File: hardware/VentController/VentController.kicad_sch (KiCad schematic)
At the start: 21 parts

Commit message: Better labels
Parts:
- C1: value (none) -> 1uF; footprint (none) -> Capacitor_SMD:C_0805_2012Metric_Pad1.18x1.45mm_HandSolder
- C2: value (none) -> .1uF; footprint (none) -> Capacitor_SMD:C_0805_2012Metric_Pad1.18x1.45mm_HandSolder
- C3: footprint (none) -> Capacitor_SMD:C_0805_2012Metric_Pad1.18x1.45mm_HandSolder
- H1: value (none) -> MountingHole_Pad; footprint (none) -> MountingHole:MountingHole_2.5mm_Pad
- H2: footprint (none) -> MountingHole:MountingHole_2.5mm_Pad
- J1: value (none) -> AM2301B; footprint (none) -> Connector_PinHeader_2.54mm:PinHeader_1x04_P2.54mm_Vertical
- J2: value (none) -> Conn_01x02; footprint (none) -> Connector_PinHeader_2.54mm:PinHeader_1x02_P2.54mm_Vertical
- J3: value (none) -> Barrel_Jack_Switch; footprint (none) -> Connector_BarrelJack:BarrelJack_Horizontal
- Q1: value (none) -> Q_NPN_EBC; footprint (none) -> Package_TO_SOT_THT:TO-92_Inline
- R1, R2: value (none) -> 4.7k; footprint (none) -> Resistor_SMD:R_0805_2012Metric_Pad1.20x1.40mm_HandSolder
- R3: value (none) -> 470; footprint (none) -> Resistor_SMD:R_0805_2012Metric_Pad1.20x1.40mm_HandSolder
- R4: value (none) -> 150; footprint (none) -> Resistor_SMD:R_0805_2012Metric_Pad1.20x1.40mm_HandSolder
- R5: value (none) -> 330
- R6: value (none) -> 0; footprint (none) -> Resistor_SMD:R_0805_2012Metric_Pad1.20x1.40mm_HandSolder
- R7, R8: value (none) -> 0
- RV1: value (none) -> 10k; footprint (none) -> Connector_PinHeader_2.54mm:PinHeader_1x03_P2.54mm_Vertical
- U1: value (none) -> ATtiny85-20P; footprint (none) -> Package_DIP:DIP-8_W7.62mm
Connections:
- net SCL renamed SCL White
- net SDA renamed SDA Yellow
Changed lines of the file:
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@@
     (effects (font (size 1.27 1.27)) (justify left bottom))
   )
-  (label "SCL" (at 80.01 39.37 0)
+  (label "SCL White" (at 78.74 39.37 0)
     (effects (font (size 1.27 1.27)) (justify left bottom))
   )
-  (label "SDA" (at 80.01 34.29 0)
+  (label "SDA Yellow" (at 78.74 34.29 0)
     (effects (font (size 1.27 1.27)) (justify left bottom))
   )
@@
     (in_bom yes) (on_board yes) (fields_autoplaced)
     (property "Reference" "R5" (id 0) (at 109.22 51.1642 90))
-    (property "Value" "" (id 1) (at 109.22 53.7011 90))
+    (property "Value" "330" (id 1) (at 109.22 53.7011 90))
     (property "Footprint" "Resistor_SMD:R_0805_2012Metric_Pad1.20x1.40mm_HandSolder" (id 2) (at 109.22 57.658 90)
       (effects (font (size 1.27 1.27)) hide)
@@
       (effects (font (size 1.27 1.27)) hide)
     )
-    (property "Value" "" (id 1) (at 26.67 92.0734 0))
+    (property "Value" "GND" (id 1) (at 26.67 92.0734 0))
     (property "Footprint" "" (id 2) (at 26.67 87.63 0)
       (effects (font (size 1.27 1.27)) hide)
@@
     (in_bom yes) (on_board yes) (fields_autoplaced)
     (property "Reference" "R3" (id 0) (at 125.73 68.9442 90))
-    (property "Value" "" (id 1) (at 125.73 71.4811 90))
-    (property "Footprint" "" (id 2) (at 125.73 75.438 90)
+    (property "Value" "470" (id 1) (at 125.73 71.4811 90))
+    (property "Footprint" "Resistor_SMD:R_0805_2012Metric_Pad1.20x1.40mm_HandSolder" (id 2) (at 125.73 75.438 90)
       (effects (font (size 1.27 1.27)) hide)
     )
@@
       (effects (font (size 1.27 1.27)) (justify left))
     )
-    (property "Value" "" (id 1) (at 138.938 52.5022 0)
-      (effects (font (size 1.27 1.27)) (justify left))
-    )
-    (property "Footprint" "" (id 2) (at 135.382 50.8 90)
+    (property "Value" "150" (id 1) (at 138.938 52.5022 0)
+      (effects (font (size 1.27 1.27)) (justify left))
+    )
+    (property "Footprint" "Resistor_SMD:R_0805_2012Metric_Pad1.20x1.40mm_HandSolder" (id 2) (at 135.382 50.8 90)
       (effects (font (size 1.27 1.27)) hide)
     )
@@
     (in_bom yes) (on_board yes) (fields_autoplaced)
     (property "Reference" "J3" (id 0) (at 44.45 102.9802 0))
-    (property "Value" "" (id 1) (at 44.45 105.5171 0))
-    (property "Footprint" "" (id 2) (at 45.72 111.506 0)
+    (property "Value" "Barrel_Jack_Switch" (id 1) (at 44.45 105.5171 0))
+    (property "Footprint" "Connector_BarrelJack:BarrelJack_Horizontal" (id 2) (at 45.72 111.506 0)
       (effects (font (size 1.27 1.27)) hide)
     )
@@
       (effects (font (size 1.27 1.27)) (justify left))
     )
-    (property "Value" "" (id 1) (at 154.432 61.7978 0)
+    (property "Value" "0" (id 1) (at 154.432 61.7978 0)
       (effects (font (size 1.27 1.27)) (justify left))
     )
@@
       (effects (font (size 1.27 1.27)) (justify left))
     )
-    (property "Value" "" (id 1) (at 89.408 29.6422 0)
-      (effects (font (size 1.27 1.27)) (justify left))
-    )
-    (property "Footprint" "" (id 2) (at 85.852 27.94 90)
+    (property "Value" "4.7k" (id 1) (at 89.408 29.6422 0)
+      (effects (font (size 1.27 1.27)) (justify left))
+    )
+    (property "Footprint" "Resistor_SMD:R_0805_2012Metric_Pad1.20x1.40mm_HandSolder" (id 2) (at 85.852 27.94 90)
       (effects (font (size 1.27 1.27)) hide)
     )
@@
       (effects (font (size 1.27 1.27)) (justify left))
     )
-    (property "Footprint" "" (id 2) (at 123.19 95.25 0)
+    (property "Footprint" "MountingHole:MountingHole_2.5mm_Pad" (id 2) (at 123.19 95.25 0)
       (effects (font (size 1.27 1.27)) hide)
     )
@@
       (effects (font (size 1.27 1.27)) (justify right))
     )
-    (property "Value" "" (id 1) (at 48.768 43.6122 0)
+    (property "Value" "ATtiny85-20P" (id 1) (at 48.768 43.6122 0)
       (effects (font (size 1.27 1.27)) (justify right))
     )
-    (property "Footprint" "" (id 2) (at 62.23 41.91 0)
+    (property "Footprint" "Package_DIP:DIP-8_W7.62mm" (id 2) (at 62.23 41.91 0)
       (effects (font (size 1.27 1.27) italic) hide)
     )
@@
       (effects (font (size 1.27 1.27)) (justify left))
     )
-    (property "Value" "" (id 1) (at 97.028 29.6422 0)
-      (effects (font (size 1.27 1.27)) (justify left))
-    )
-    (property "Footprint" "" (id 2) (at 93.472 27.94 90)
+    (property "Value" "4.7k" (id 1) (at 97.028 29.6422 0)
+      (effects (font (size 1.27 1.27)) (justify left))
+    )
+    (property "Footprint" "Resistor_SMD:R_0805_2012Metric_Pad1.20x1.40mm_HandSolder" (id 2) (at 93.472 27.94 90)
       (effects (font (size 1.27 1.27)) hide)
     )
@@
       (effects (font (size 1.27 1.27)) (justify left))
     )
-    (property "Value" "" (id 1) (at 102.87 95.6822 0)
-      (effects (font (size 1.27 1.27)) (justify left))
-    )
-    (property "Footprint" "" (id 2) (at 100.33 95.25 0)
+    (property "Value" "MountingHole_Pad" (id 1) (at 102.87 95.6822 0)
+      (effects (font (size 1.27 1.27)) (justify left))
+    )
+    (property "Footprint" "MountingHole:MountingHole_2.5mm_Pad" (id 2) (at 100.33 95.25 0)
       (effects (font (size 1.27 1.27)) hide)
     )
@@
       (effects (font (size 1.27 1.27)) hide)
     )
-    (property "Value" "" (id 1) (at 43.18 76.4342 0))
+    (property "Value" "VCC" (id 1) (at 43.18 76.4342 0))
     (property "Footprint" "" (id 2) (at 43.18 80.01 0)
       (effects (font (size 1.27 1.27)) hide)
@@
       (effects (font (size 1.27 1.27)) (justify left))
     )
-    (property "Value" "" (id 1) (at 46.101 85.5222 0)
-      (effects (font (size 1.27 1.27)) (justify left))
-    )
-    (property "Footprint" "" (id 2) (at 44.1452 87.63 0)
+    (property "Value" ".1uF" (id 1) (at 46.101 85.5222 0)
+      (effects (font (size 1.27 1.27)) (justify left))
+    )
+    (property "Footprint" "Capacitor_SMD:C_0805_2012Metric_Pad1.18x1.45mm_HandSolder" (id 2) (at 44.1452 87.63 0)
       (effects (font (size 1.27 1.27)) hide)
     )
@@
       (effects (font (size 1.27 1.27)) (justify left))
     )
-    (property "Value" "" (id 1) (at 146.558 65.2022 0)
+    (property "Value" "0" (id 1) (at 146.558 65.2022 0)
       (effects (font (size 1.27 1.27)) (justify left))
     )
@@
       (effects (font (size 1.27 1.27)) (justify left))
     )
-    (property "Value" "" (id 1) (at 138.938 63.9322 0)
-      (effects (font (size 1.27 1.27)) (justify left))
-    )
-    (property "Footprint" "" (id 2) (at 135.382 62.23 90)
+    (property "Value" "0" (id 1) (at 138.938 63.9322 0)
+      (effects (font (size 1.27 1.27)) (justify left))
+    )
+    (property "Footprint" "Resistor_SMD:R_0805_2012Metric_Pad1.20x1.40mm_HandSolder" (id 2) (at 135.382 62.23 90)
       (effects (font (size 1.27 1.27)) hide)
     )
@@
       (effects (font (size 1.27 1.27)) (justify left))
     )
-    (property "Value" "" (id 1) (at 139.4714 75.3622 0)
-      (effects (font (size 1.27 1.27)) (justify left))
-    )
-    (property "Footprint" "" (id 2) (at 139.7 71.12 0)
+    (property "Value" "Q_NPN_EBC" (id 1) (at 139.4714 75.3622 0)
+      (effects (font (size 1.27 1.27)) (justify left))
+    )
+    (property "Footprint" "Package_TO_SOT_THT:TO-92_Inline" (id 2) (at 139.7 71.12 0)
       (effects (font (size 1.27 1.27)) hide)
     )
@@
       (effects (font (size 1.27 1.27)) (justify left))
     )
-    (property "Value" "" (id 1) (at 111.252 42.3422 0)
-      (effects (font (size 1.27 1.27)) (justify left))
-    )
-    (property "Footprint" "" (id 2) (at 109.22 39.37 0)
+    (property "Value" "AM2301B" (id 1) (at 111.252 42.3422 0)
+      (effects (font (size 1.27 1.27)) (justify left))
+    )
+    (property "Footprint" "Connector_PinHeader_2.54mm:PinHeader_1x04_P2.54mm_Vertical" (id 2) (at 109.22 39.37 0)
       (effects (font (size 1.27 1.27)) hide)
     )
@@
       (effects (font (size 1.27 1.27)) (justify left))
     )
-    (property "Footprint" "" (id 2) (at 59.3852 87.63 0)
+    (property "Footprint" "Capacitor_SMD:C_0805_2012Metric_Pad1.18x1.45mm_HandSolder" (id 2) (at 59.3852 87.63 0)
       (effects (font (size 1.27 1.27)) hide)
     )
@@
       (effects (font (size 1.27 1.27)) (justify right))
     )
-    (property "Value" "" (id 1) (at 114.808 63.9322 0)
+    (property "Value" "10k" (id 1) (at 114.808 63.9322 0)
       (effects (font (size 1.27 1.27)) (justify right))
     )
-    (property "Footprint" "" (id 2) (at 113.03 62.23 0)
+    (property "Footprint" "Connector_PinHeader_2.54mm:PinHeader_1x03_P2.54mm_Vertical" (id 2) (at 113.03 62.23 0)
       (effects (font (size 1.27 1.27)) hide)
     )
@@
       (effects (font (size 1.27 1.27)) (justify left))
     )
-    (property "Value" "" (id 1) (at 168.402 60.1222 0)
-      (effects (font (size 1.27 1.27)) (justify left))
-    )
-    (property "Footprint" "" (id 2) (at 166.37 57.15 0)
+    (property "Value" "Conn_01x02" (id 1) (at 168.402 60.1222 0)
+      (effects (font (size 1.27 1.27)) (justify left))
+    )
+    (property "Footprint" "Connector_PinHeader_2.54mm:PinHeader_1x02_P2.54mm_Vertical" (id 2) (at 166.37 57.15 0)
       (effects (font (size 1.27 1.27)) hide)
     )
@@
       (effects (font (size 1.27 1.27)) hide)
     )
-    (property "Value" "" (id 1) (at 63.5 117.4734 0))
+    (property "Value" "PWR_FLAG" (id 1) (at 63.5 117.4734 0))
     (property "Footprint" "" (id 2) (at 63.5 113.03 0)
       (effects (font (size 1.27 1.27)) hide)
@@
       (effects (font (size 1.27 1.27)) (justify left))
     )
-    (property "Value" "" (id 1) (at 29.591 85.5222 0)
-      (effects (font (size 1.27 1.27)) (justify left))
-    )
-    (property "Footprint" "" (id 2) (at 27.6352 87.63 0)
-      (effects (font (size 1.27 1.27)) hide)
-    )
+    (property "Value" "1uF" (id 1) (at 29.591 85.5222 0)
+      (effects (font (size 1.27 1.27)) (justify left))
+    )
+    (property "Footprint" "Capacitor_SMD:C_0805_2012Metric_Pad1.18x1.45mm_HandSolder" (id 2) (at 27.6352 87.63 0)
+      (effects (font (size 1.27 1.27)) hide)
+    )

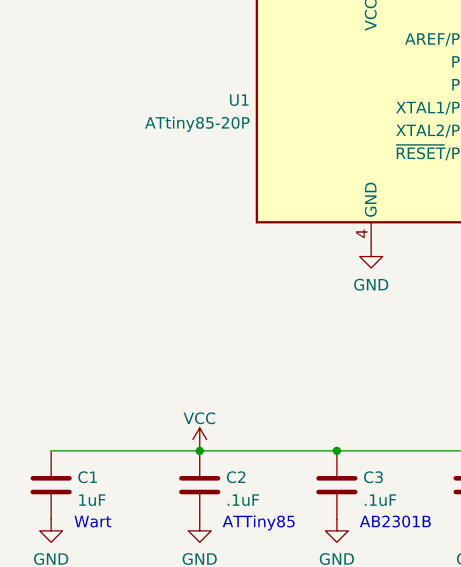
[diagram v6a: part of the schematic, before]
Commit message: Feedback from board
* Added power led
* Updated text
* Adjusted mounting hole layout
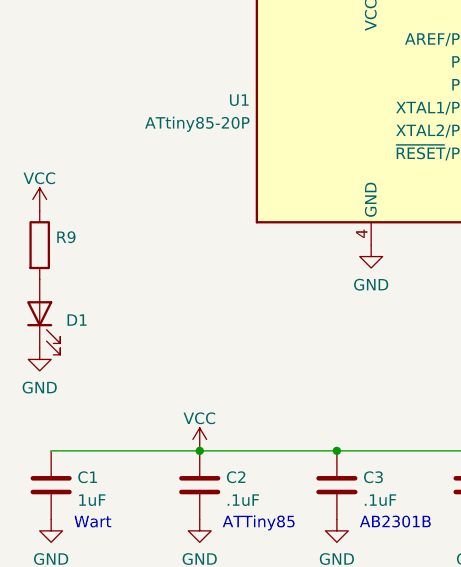
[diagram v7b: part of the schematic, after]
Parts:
- added D1: (no value), symbol Device:LED
- added R9: (no value), symbol Device:R
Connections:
- net GND: now also D1.1 (K)
- net VCC: now also R9.1
- new net: D1.2 (A), R9.2
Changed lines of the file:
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@@
     (pin "8")
+  )
+  (symbol (lib_id "power:GND") (at 25.4 68.58 0) (unit 1)
+    (in_bom yes) (on_board yes) (fields_autoplaced)
+    (property "Reference" "#PWR020" (id 0) (at 25.4 74.93 0)
+      (effects (font (size 1.27 1.27)) hide)
+    )
+    (property "Value" "GND" (id 1) (at 25.4 73.0234 0))
+    (property "Footprint" "" (id 2) (at 25.4 68.58 0)
+      (effects (font (size 1.27 1.27)) hide)
+    )
+    (property "Datasheet" "" (id 3) (at 25.4 68.58 0)
+      (effects (font (size 1.27 1.27)) hide)
+    )
+    (pin "1")
   )
   (symbol (lib_id "Device:R") (at 95.25 27.94 0) (unit 1)
@@
     )
     (property "Datasheet" "" (id 3) (at 137.16 78.74 0)
+      (effects (font (size 1.27 1.27)) hide)
+    )
+    (pin "1")
+  )
+  (symbol (lib_id "power:VCC") (at 25.4 53.34 0) (unit 1)
+    (in_bom yes) (on_board yes) (fields_autoplaced)
+    (property "Reference" "#PWR019" (id 0) (at 25.4 57.15 0)
+      (effects (font (size 1.27 1.27)) hide)
+    )
+    (property "Value" "VCC" (id 1) (at 25.4 49.7642 0))
+    (property "Footprint" "" (id 2) (at 25.4 53.34 0)
+      (effects (font (size 1.27 1.27)) hide)
+    )
+    (property "Datasheet" "" (id 3) (at 25.4 53.34 0)
       (effects (font (size 1.27 1.27)) hide)
     )
@@
     (pin "3")
   )
+  (symbol (lib_id "Device:R") (at 25.4 57.15 0) (unit 1)
+    (in_bom yes) (on_board yes) (fields_autoplaced)
+    (property "Reference" "R9" (id 0) (at 27.178 56.3153 0)
+      (effects (font (size 1.27 1.27)) (justify left))
+    )
+    (property "Value" "" (id 1) (at 27.178 58.8522 0)
+      (effects (font (size 1.27 1.27)) (justify left))
+    )
+    (property "Footprint" "" (id 2) (at 23.622 57.15 90)
+      (effects (font (size 1.27 1.27)) hide)
+    )
+    (property "Datasheet" "~" (id 3) (at 25.4 57.15 0)
+      (effects (font (size 1.27 1.27)) hide)
+    )
+    (pin "1")
+    (pin "2")
+  )
   (symbol (lib_id "power:VCC") (at 105.41 55.88 90) (unit 1)
     (in_bom yes) (on_board yes) (fields_autoplaced)
@@
     )
     (property "Datasheet" "~" (id 3) (at 58.42 83.82 0)
+      (effects (font (size 1.27 1.27)) hide)
+    )
+    (pin "1")
+    (pin "2")
+  )
+  (symbol (lib_id "Device:LED") (at 25.4 64.77 90) (unit 1)
+    (in_bom yes) (on_board yes) (fields_autoplaced)
+    (property "Reference" "D1" (id 0) (at 28.321 65.5228 90)
+      (effects (font (size 1.27 1.27)) (justify right))
+    )
+    (property "Value" "" (id 1) (at 28.321 68.0597 90)
+      (effects (font (size 1.27 1.27)) (justify right))
+    )
+    (property "Footprint" "" (id 2) (at 25.4 64.77 0)
+      (effects (font (size 1.27 1.27)) hide)
+    )
+    (property "Datasheet" "~" (id 3) (at 25.4 64.77 0)
       (effects (font (size 1.27 1.27)) hide)
     )
@@
       (reference "#PWR018") (unit 1) (value "GND") (footprint "")
     )
+    (path "/6f2a61dd-5d58-4f9a-947c-9eede02ebaf9"
+      (reference "#PWR019") (unit 1) (value "VCC") (footprint "")
+    )
+    (path "/54d1b8c5-e296-4acb-b9b5-05aa59a1a85b"
+      (reference "#PWR020") (unit 1) (value "GND") (footprint "")
+    )
     (path "/65b883a7-f8ee-466f-b815-3a02492bdf71"
       (reference "#PWR0101") (unit 1) (value "GND") (footprint "")
@@
       (reference "C5") (unit 1) (value ".1uF") (footprint "Capacitor_SMD:C_0805_2012Metric_Pad1.18x1.45mm_HandSolder")
     )
+    (path "/aff00d57-63ea-46b6-99f8-32eff51e9707"
+      (reference "D1") (unit 1) (value "Power LED") (footprint "LED_SMD:LED_0805_2012Metric_Pad1.15x1.40mm_HandSolder")
+    )
     (path "/60ad6398-c6b2-4e4f-8f74-2f6a7e07b594"
       (reference "H1") (unit 1) (value "MountingHole_Pad") (footprint "MountingHole:MountingHole_2.5mm_Pad")
@@
       (reference "R8") (unit 1) (value "0") (footprint "Resistor_SMD:R_0805_2012Metric_Pad1.20x1.40mm_HandSolder")
     )
+    (path "/9083f655-5a58-4b7a-9ae9-5736a88fdadc"
+      (reference "R9") (unit 1) (value "330") (footprint "Resistor_SMD:R_0805_2012Metric_Pad1.20x1.40mm_HandSolder")
+    )
     (path "/db7b86be-d02f-4f2d-9a67-25a0b7eb5f5e"
